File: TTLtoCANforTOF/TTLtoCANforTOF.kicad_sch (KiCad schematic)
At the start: 44 parts, among them J1 CAN, J2 STP-23L, J4 XT30, J5 SWD, SW1 SW_SPST, U1 TPS54202DDC, U2 ME6211C33M5, U3 STM32G0B1CBTx, U6 TCAN3413DR, Y1 X32258MSB

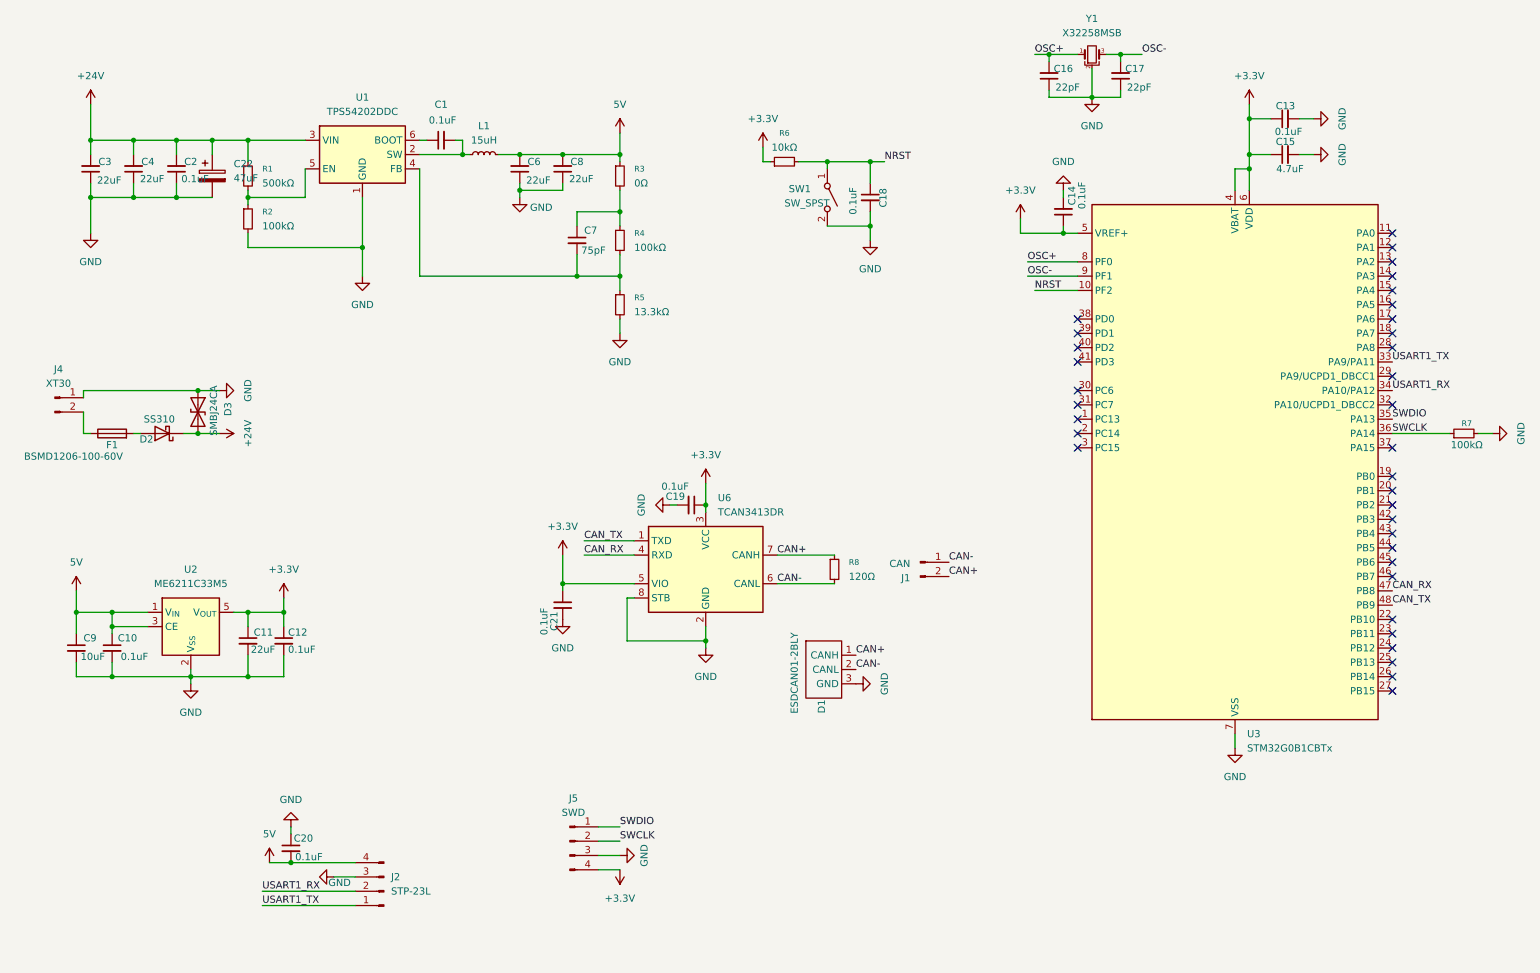
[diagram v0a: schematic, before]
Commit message: 修改了保护电路
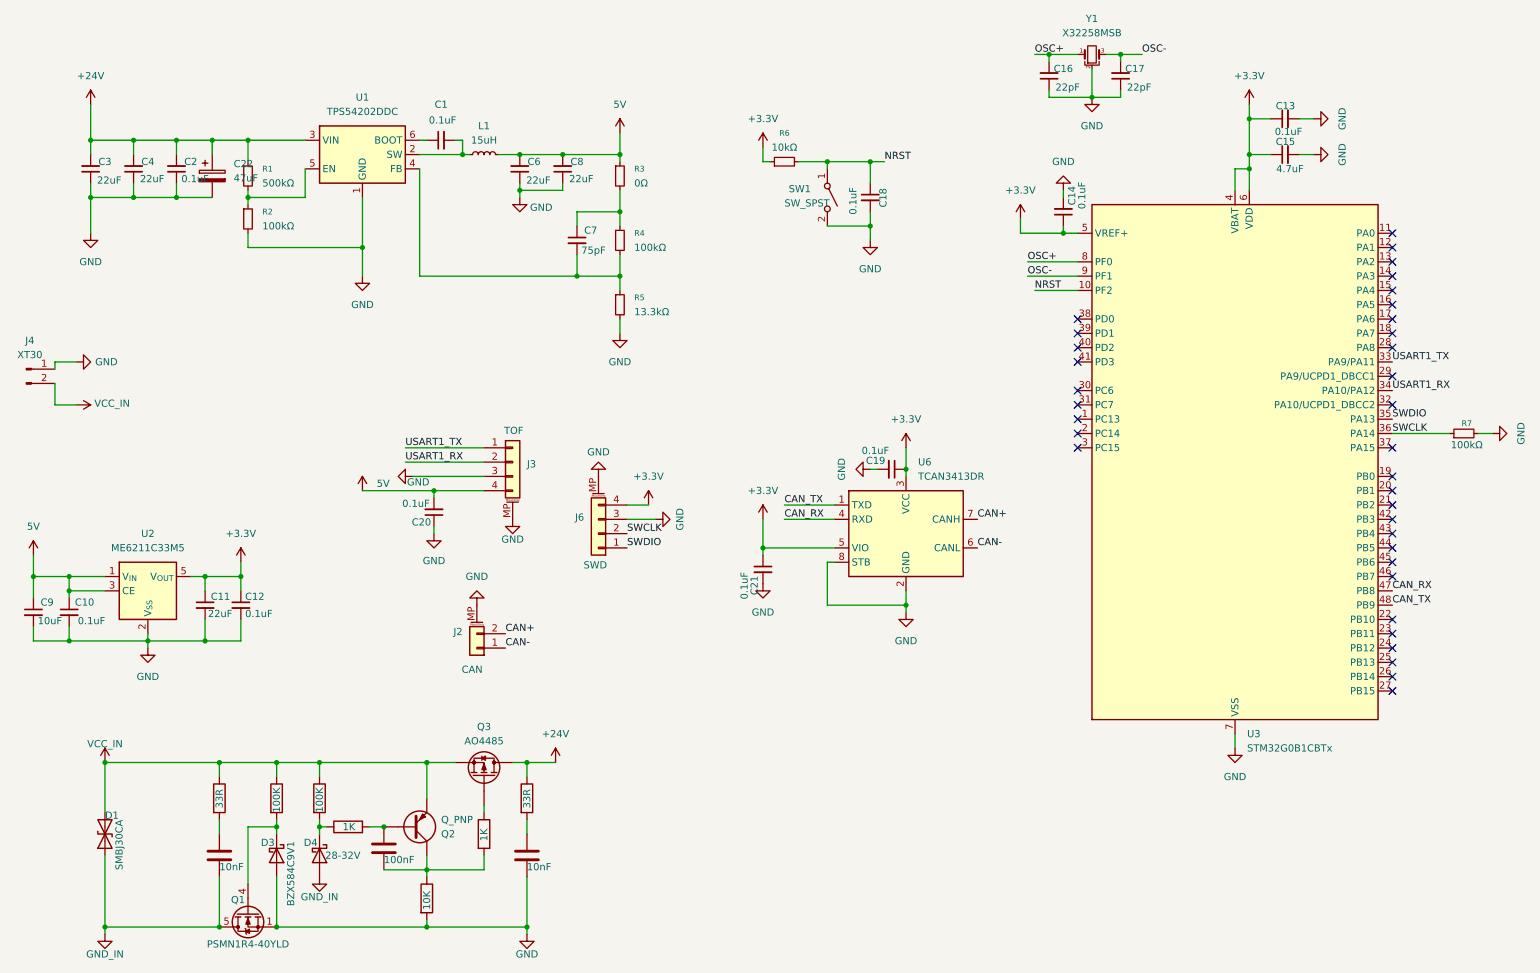
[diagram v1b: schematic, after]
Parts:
- removed D1: ESDCAN01-2BLY, Package_TO_SOT_SMD:SOT-23-3, symbol aaaa:PESD1CAN
- removed D2: SS310, Diode_SMD:D_SMA, symbol Device:D_Schottky
- removed D3: SMBJ24CA, Diode_SMD:D_SMB, symbol Device:D_TVS
- removed F1: BSMD1206-100-60V, Fuse:Fuse_1206_3216Metric, symbol Device:Fuse
- removed J1: CAN, Connector_JST:JST_GH_SM02B-GHS-TB_1x02-1MP_P1.25mm_Horizontal, symbol Connector:Conn_01x02_Pin
- removed J2: STP-23L, Connector_JST:JST_GH_SM04B-GHS-TB_1x04-1MP_P1.25mm_Horizontal, symbol Connector:Conn_01x04_Pin
- removed J5: SWD, Connector_Molex:Molex_CLIK-Mate_502386-0470_1x04-1MP_P1.25mm_Horizontal, symbol Connector:Conn_01x04_Pin
- removed R8: 120Ω, Resistor_SMD:R_1206_3216Metric, symbol Device:R_Small
- added C23: 100nF, Capacitor_SMD:C_0603_1608Metric, symbol Device:C
- added C24, C5: 10nF, Capacitor_SMD:C_0603_1608Metric, symbol Device:C
- added D1: SMBJ30CA, Diode_SMD:D_SMB, symbol Device:D_TVS
- added D3: BZX584C9V1, Diode_SMD:D_SOD-523, symbol Device:D_Schottky
- added D4: 28-32V, Diode_SMD:D_SOD-523, symbol Device:D_Schottky
- added J2: CAN, Connector_JST:JST_GH_SM02B-GHS-TB_1x02-1MP_P1.25mm_Horizontal, symbol Connector_Generic_MountingPin:Conn_01x02_MountingPin
- added J3: TOF, Connector_JST:JST_GH_SM04B-GHS-TB_1x04-1MP_P1.25mm_Horizontal, symbol Connector_Generic_MountingPin:Conn_01x04_MountingPin
- added J6: SWD, Connector_Molex:Molex_CLIK-Mate_502386-0470_1x04-1MP_P1.25mm_Horizontal, symbol Connector_Generic_MountingPin:Conn_01x04_MountingPin
- added Q1: PSMN1R4-40YLD, Package_TO_SOT_SMD:LFPAK56, symbol Transistor_FET:PSMN5R2-60YL
- added Q2: Q_PNP, Package_TO_SOT_SMD:SOT-23, symbol Device:Q_PNP
- added Q3: AO4485, Package_SO:SOP-8_3.76x4.96mm_P1.27mm, symbol Device:Q_PMOS
- added R10, R9: 100K, Resistor_SMD:R_0603_1608Metric, symbol Device:R
- added R11, R13: 1K, Resistor_SMD:R_0603_1608Metric, symbol Device:R
- added R12: 10K, Resistor_SMD:R_0603_1608Metric, symbol Device:R
- added R14, R8: 33R, Resistor_SMD:R_0603_1608Metric, symbol Device:R
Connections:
- net +24V: now also Q3.5 (D), Q3.6 (D), Q3.7 (D), Q3.8 (D), R14.1
- net +3.3V: now also J6.4 (Pin_4)
- net 5V: now also J3.4 (Pin_4)
- net CAN+: now also J2.2 (Pin_2)
- net CAN-: now also J2.1 (Pin_1)
- net GND: now also C24.2, D3.2 (A), J2.MP (MountPin), J3.3 (Pin_3), J3.MP (MountPin), J6.3 (Pin_3), J6.MP (MountPin), Q1.1 (S), Q1.2 (S), Q1.3 (S), R12.2
- net SWCLK: now also J6.2 (Pin_2)
- net SWDIO: now also J6.1 (Pin_1)
- net USART1_RX: now also J3.2 (Pin_2)
- net USART1_TX: now also J3.1 (Pin_1)
- net VCC_IN: now reaches J4.2 (Pin_2)
- net VCC_IN: now also D1.2 (A2), Q2.E, Q3.1 (S), Q3.2 (S), Q3.3 (S), R10.1, R8.1, R9.1
- new net: C5.1, R8.2
- new net: D4.1 (K), R10.2, R11.1
- new net: C23.1, Q2.B, R11.2
- new net: Q3.4 (G), R13.1
- new net: C23.2, Q2.C, R12.1, R13.2
- new net: D3.1 (K), Q1.4 (G), R9.2
- new net: C24.1, R14.2
- new net GND_IN: C5.2, D1.1 (A1), D4.2 (A), Q1.5 (D)
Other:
- moved on the sheet: C10, C11, C12, C19, C20, C21, C9, J4, U2, U6
